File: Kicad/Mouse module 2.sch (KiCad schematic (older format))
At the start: 29 parts, among them J1 Conn_02x20_Odd_Even, J2 02x08_IDC, J3 AudioJack3, J4 AudioJack3, J5 AudioJack3, J6 AudioJack3, J7 AudioJack3, U1 74LS125, U2 TL072, U3 MCP4922

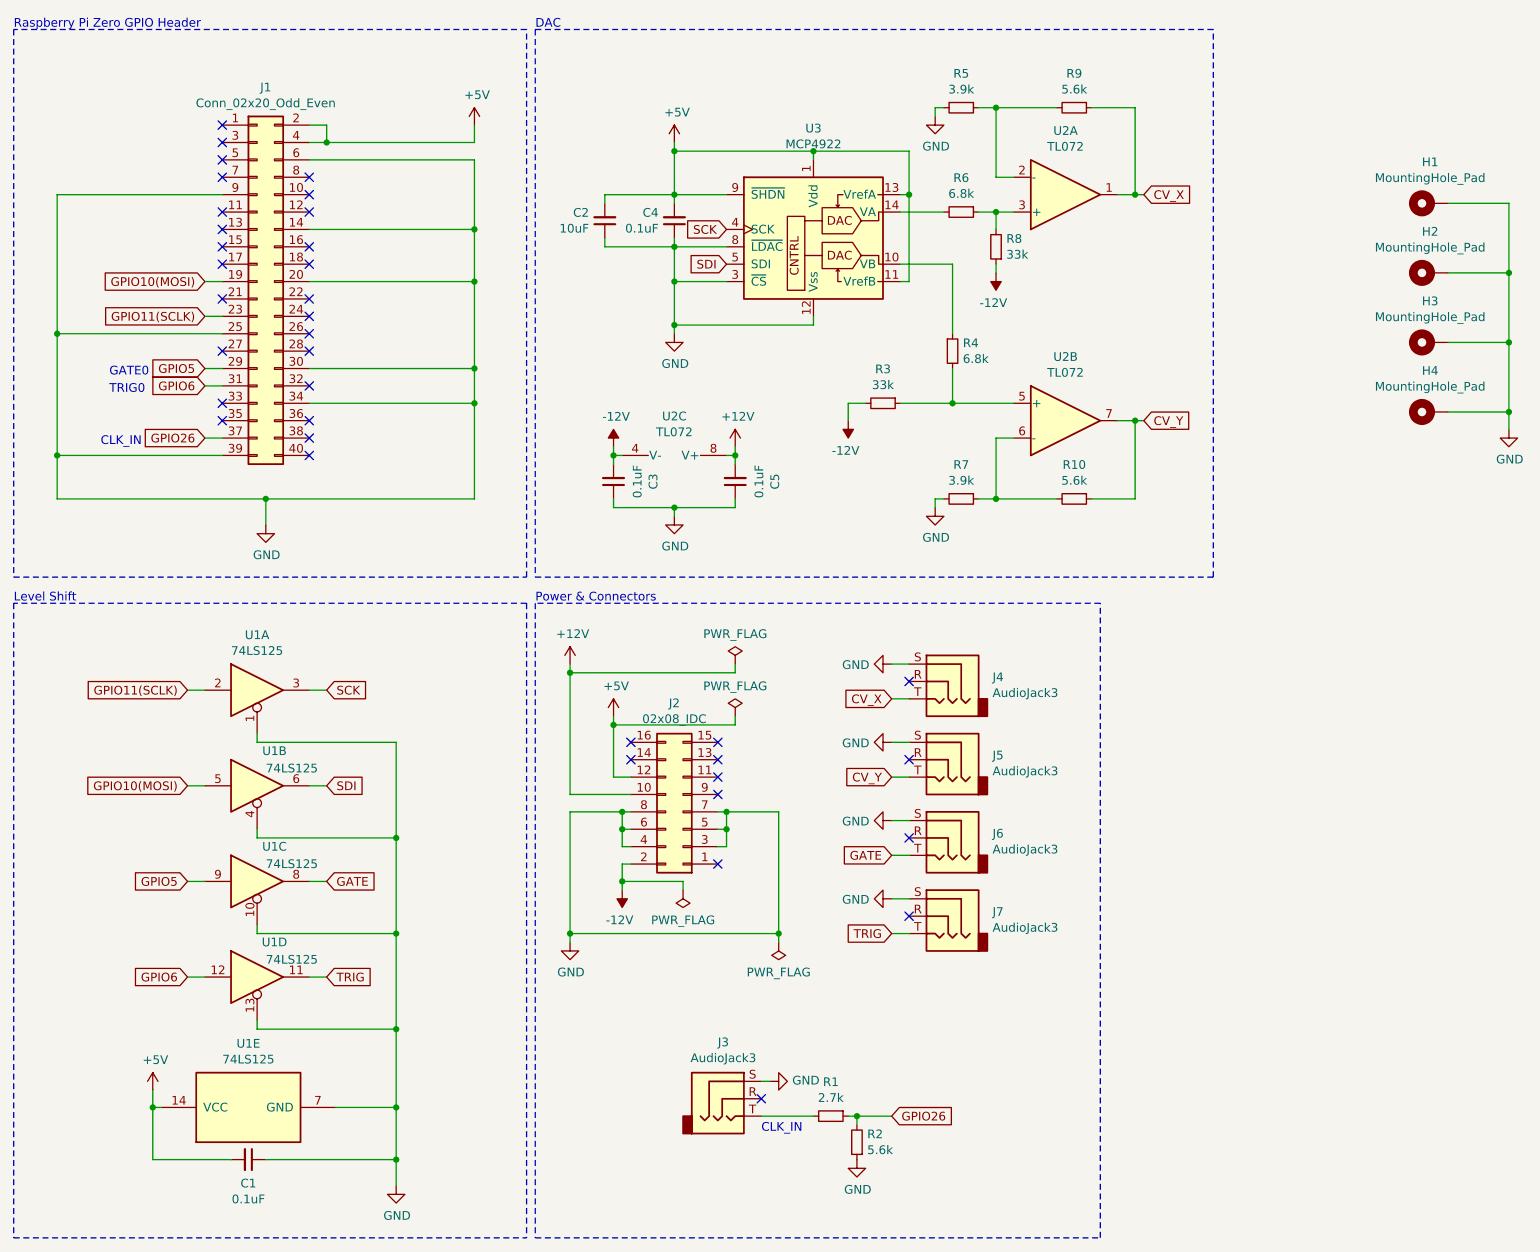
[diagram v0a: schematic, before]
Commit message: removed DAC from schematics
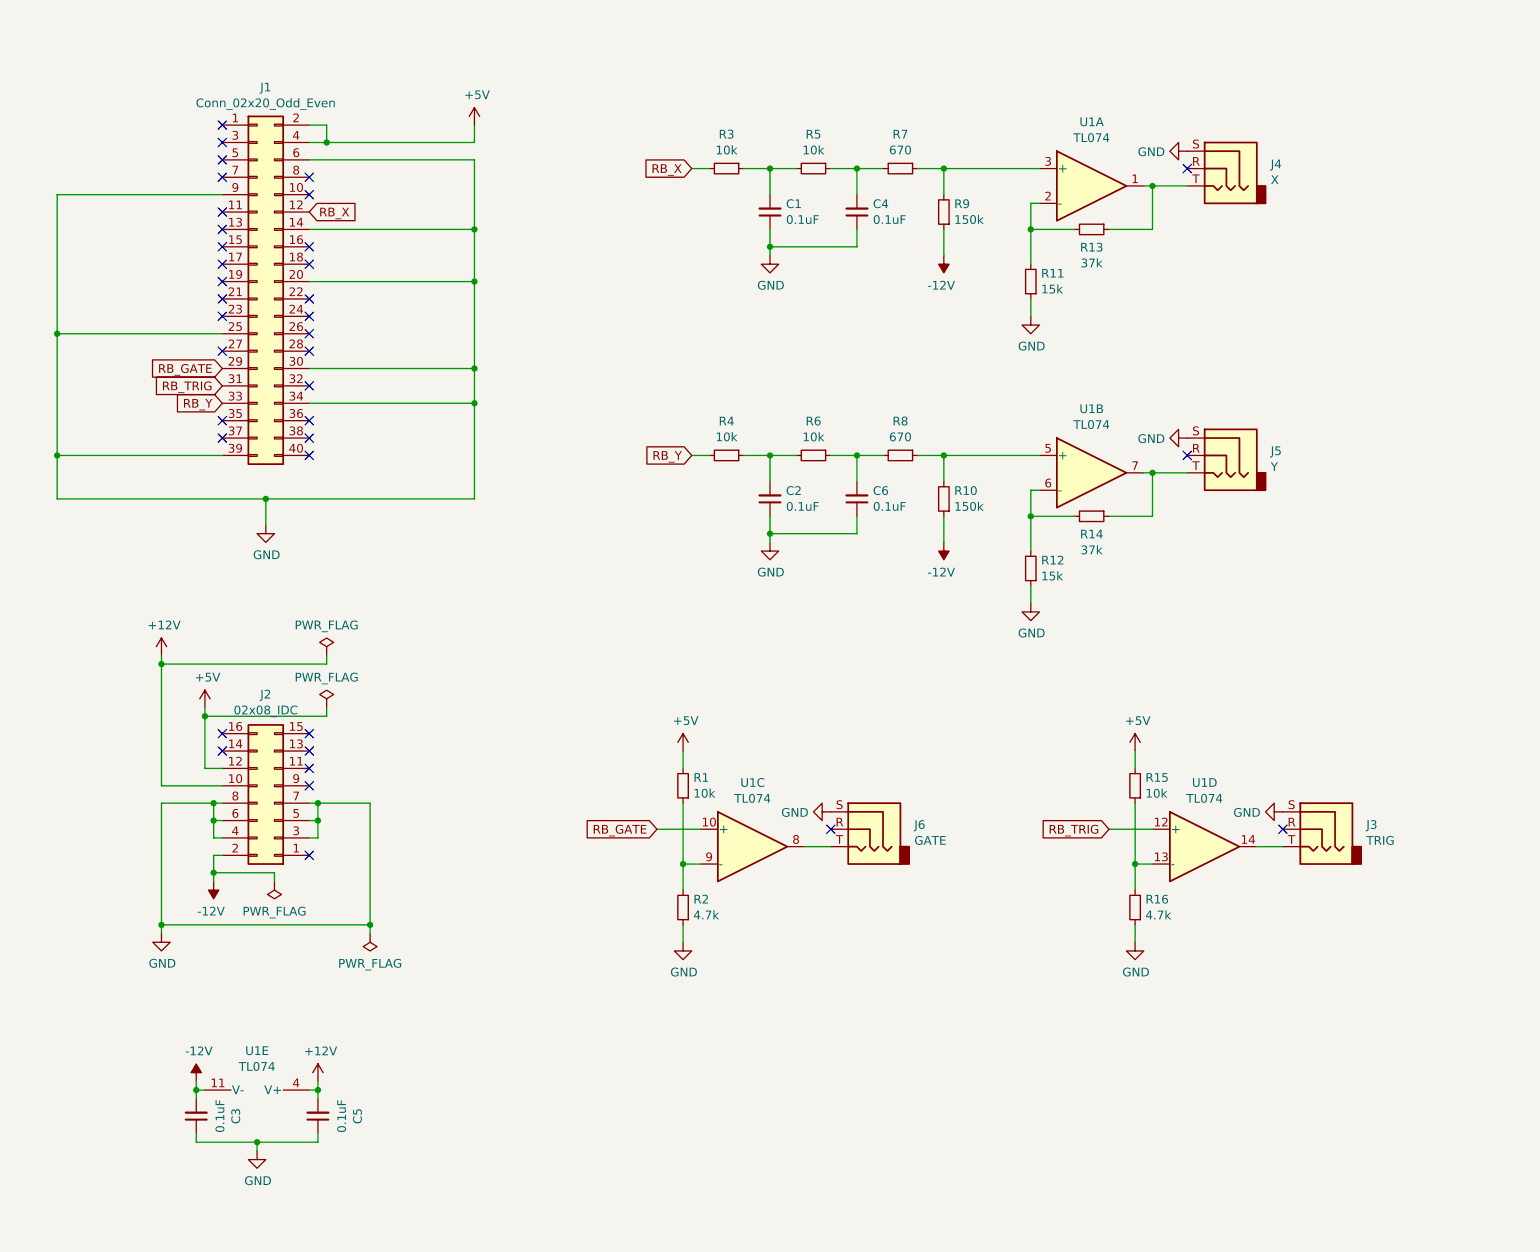
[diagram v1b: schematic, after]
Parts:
- removed H1, H2, H3, H4: MountingHole_Pad, MountingHole:MountingHole_2.7mm_Pad, symbol Mechanical:MountingHole_Pad
- removed J7: AudioJack3, SJ1-3533:CUI_SJ1-3533, symbol Connector:AudioJack3
- removed U1: 74LS125, Package_DIP:DIP-14_W7.62mm_Socket, symbol 74xx:74LS125
- removed U2: TL072, Package_DIP:DIP-8_W7.62mm_Socket, symbol Amplifier_Operational:TL072
- removed U3: MCP4922, Package_DIP:DIP-14_W7.62mm_Socket, symbol Analog_DAC:MCP4922
- added C6: 0.1uF, Capacitor_THT:C_Disc_D4.7mm_W2.5mm_P5.00mm, symbol Device:C_Small
- added R11, R12: 15k, Resistor_THT:R_Axial_DIN0207_L6.3mm_D2.5mm_P10.16mm_Horizontal, symbol Device:R_Small
- added R13, R14: 37k, Resistor_THT:R_Axial_DIN0207_L6.3mm_D2.5mm_P10.16mm_Horizontal, symbol Device:R_Small
- added R15: 10k, Resistor_THT:R_Axial_DIN0207_L6.3mm_D2.5mm_P10.16mm_Horizontal, symbol Device:R_Small
- added R16: 4.7k, Resistor_THT:R_Axial_DIN0207_L6.3mm_D2.5mm_P10.16mm_Horizontal, symbol Device:R_Small
- added U1: TL074, symbol Amplifier_Operational:TL074
- C2: value 10uF -> 0.1uF
- J3: value AudioJack3 -> TRIG
- J4: value AudioJack3 -> X
- J5: value AudioJack3 -> Y
- J6: value AudioJack3 -> GATE
- R1: value 2.7k -> 10k
- R10, R9: value 5.6k -> 150k
- R2: value 5.6k -> 4.7k
- R3: value 33k -> 10k
- R4, R6: value 6.8k -> 10k
- R5: value 3.9k -> 10k
- R7: value 3.9k -> 670
- R8: value 33k -> 670
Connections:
- net +12V: now also U1.4 (V+)
- net +5V: now also R1.2, R15.2; no longer C1.2, C2.2, C4.2
- net -12V: now also R10.1, R9.1, U1.11 (V-); no longer R3.2, R8.1
- net GND: now also C6.1, R11.1, R12.1, R16.1; no longer R5.2, R7.2
- net RB_X: now reaches J1.12 (Pin_12)
- net RB_X: now also R3.2
- net RB_Y: now reaches J1.33 (Pin_33)
- net RB_Y: now also R4.2
- net at R6.1, R8.2: now also C6.2
- net at R6.2: now also C2.2, R4.1
- net at R5.1: now also C4.2, R7.2; no longer R9.2
- net at R3.1: now also C1.2, R5.2; no longer R4.2
- net at R7.1: now also R9.2, U1.3 (+); no longer R10.2
- net at J3.T: now also U1.14; no longer R1.2
- net CV_X: no longer names the net of J4.T
- net CV_X: now also R13.1, U1.1; no longer R9.1
- net CV_Y: no longer names the net of J5.T
- net CV_Y: now also R14.1, U1.7; no longer R10.1
- net GATE: no longer names the net of J6.T
- net GATE: now also U1.8
- net GPIO10(MOSI): no longer names the net of J1.19 (Pin_19)
- net GPIO11(SCLK): no longer names the net of J1.23 (Pin_23)
- net GPIO26: no longer names the net of R1.1, R2.2
- net GPIO26: now also U1.9 (-); no longer J1.37 (Pin_37)
- net GPIO5 renamed RB_GATE
- net RB_GATE: now also U1.10 (+)
- net GPIO6 renamed RB_TRIG
- net RB_TRIG: now also U1.12 (+)
- new net: R11.2, R13.2, U1.2 (-)
- new net: R10.2, R8.1, U1.5 (+)
- new net: R12.2, R14.2, U1.6 (-)
- new net: R15.1, R16.2, U1.13 (-)
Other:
- note removed: "CLK_IN"
- note removed: "DAC"
- note removed: "GATE0"
- note removed: "Level Shift"
- note removed: "Power & Connectors"
- note removed: "Raspberry Pi Zero GPIO Header"
- note removed: "TRIG0"
- moved on the sheet: C3, C5, J2, J4, J5, J6
